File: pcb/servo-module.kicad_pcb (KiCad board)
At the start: 4 copper layers, 50 x 30 mm, 44 parts, among them J1 AVR-UPDI-6, J2 QWICC, J3 Power, J4 INPUT, J5 PWM1, J6 PWM2, J7 PWM3, J8 PWM4, U2 ATTINY1616MNR

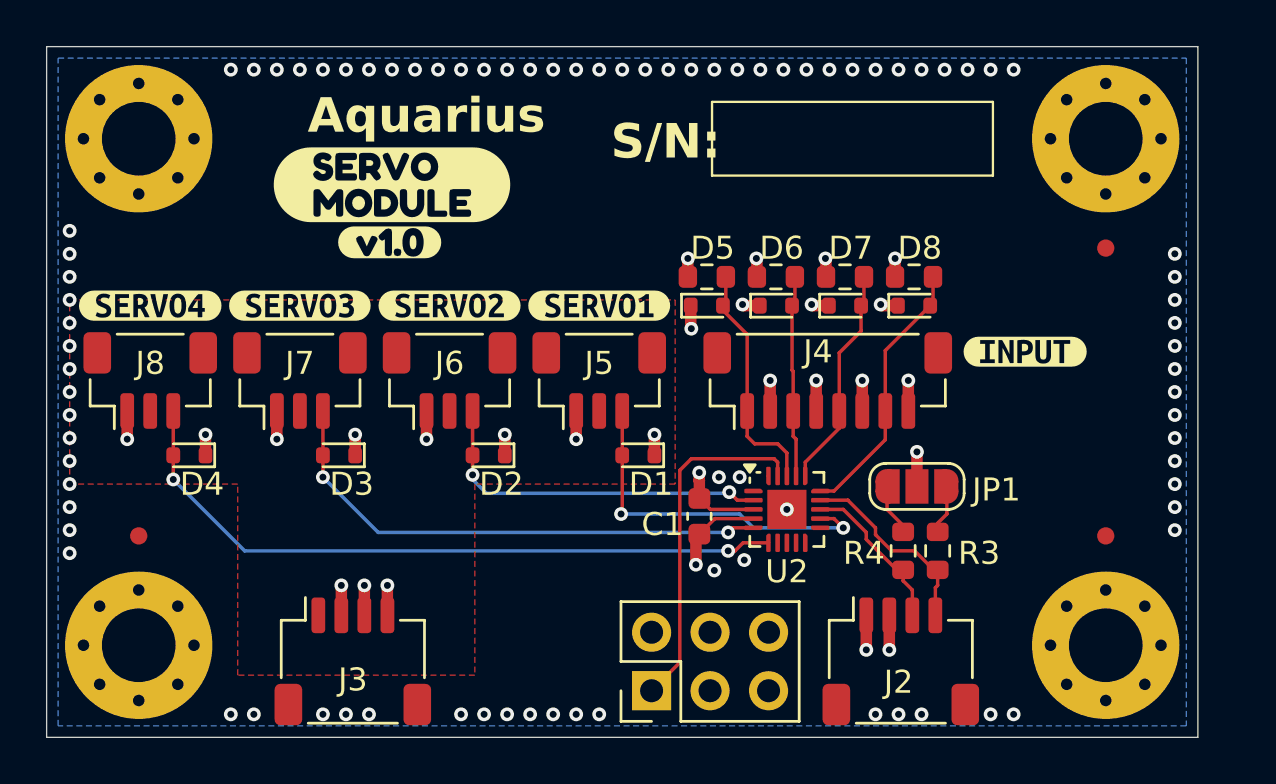
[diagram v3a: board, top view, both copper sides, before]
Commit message: Made multi-sheet; changed LEDs to WS2812; rerouted whole board
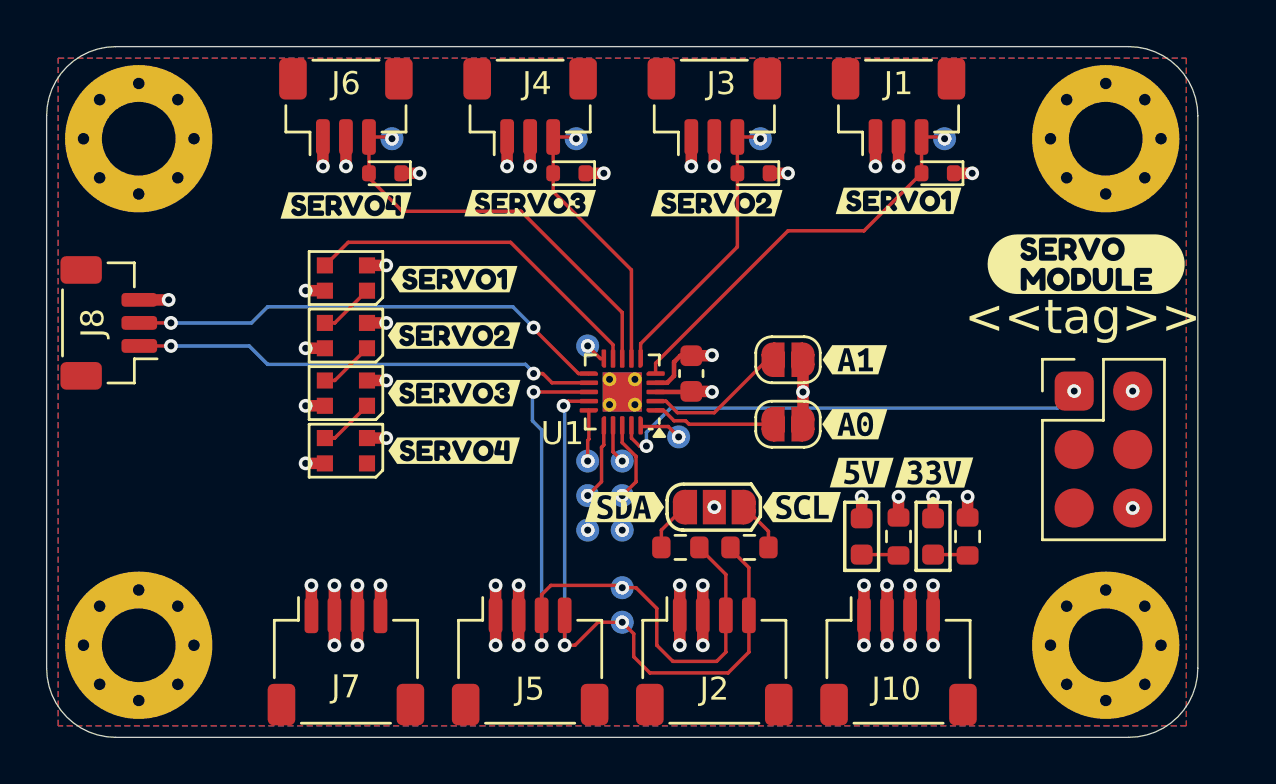
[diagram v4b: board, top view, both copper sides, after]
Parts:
- removed FID1, FID2, FID3: Fiducial, Fiducial:Fiducial_0.75mm_Mask1.5mm
- removed LOGO5: Logo_Open_Hardware_Small, Symbol:OSHW-Logo_5.7x6mm_SilkScreen
- removed R5, R6, R7, R8: 10K, Resistor_SMD:R_0603_1608Metric
- removed U2: ATTINY1616MNR, Package_DFN_QFN:VQFN-20-1EP_3x3mm_P0.4mm_EP1.7x1.7mm
- removed kibuzzard-67E4BAC2: G***, kibuzzard-67E4BAC2
- removed kibuzzard-67E4BADC: G***, kibuzzard-67E4BADC
- removed kibuzzard-67E9F1A1: G***, kibuzzard-67E9F1A1
- removed kibuzzard-67E9F1AC: G***, kibuzzard-67E9F1AC
- removed kibuzzard-67E9F1C4: G***, kibuzzard-67E9F1C4
- removed kibuzzard-67E9F26B: G***, kibuzzard-67E9F26B
- removed kibuzzard-67E9F303: G***, kibuzzard-67E9F303
- removed kibuzzard-67F88258: G***, kibuzzard-67F88258
- removed kibuzzard-67F8826B: G***, kibuzzard-67F8826B
- added D10: PESD5V0S1BB, CRGM Passive:D_SOD-523, F.Cu at (64.7, 140.5)
- added D9: PESD5V0S1BB, CRGM Passive:D_SOD-523, F.Cu at (72.7, 140.5)
- added J10: Power Out, CRGM Connector:JST_SH_SM04B-SRSS-TB_1x04-1MP_P1.00mm_Horizontal, F.Cu at (87.0, 161.7)
- added J9: AVR-UPDI-6, CRGM Connector:PinHeader_2x03_P2.54mm_Vertical_SMD, F.Cu at (94.6, 150.0)
- added JP2: A0, CRGM Connector:SolderJumper-2_P1.3mm_Open_RoundedPad1.0x1.5mm, F.Cu at (82.2, 151.4)
- added JP3: A1, CRGM Connector:SolderJumper-2_P1.3mm_Open_RoundedPad1.0x1.5mm, F.Cu at (82.2, 148.6)
- added LOGO2: ~, CRGM Logos:FNWW Face 8mm, B.Cu at (56.8, 151.9)
- added R1: 4.7K, Resistor_SMD:R_0603_1608Metric, F.Cu at (77.5, 156.8)
- added R2: 4.7K, Resistor_SMD:R_0603_1608Metric, F.Cu at (80.5, 156.8)
- added TP1: PA1, CRGM Mechanical:TestPoint_Pad_D1.0mm, B.Cu at (77.5, 151.9)
- added TP10: UPDI, CRGM Mechanical:TestPoint_Pad_D1.0mm, B.Cu at (94.6, 150.0)
- added TP11: V33, CRGM Mechanical:TestPoint_Pad_D1.0mm, B.Cu at (73.5, 156.0)
- added TP12: GND, CRGM Mechanical:TestPoint_Pad_D1.0mm, B.Cu at (75.0, 156.0)
- added TP13: PB3, CRGM Mechanical:TestPoint_Pad_D1.0mm, B.Cu at (73.5, 148.0)
- added TP14: PC3, CRGM Mechanical:TestPoint_Pad_D1.0mm, B.Cu at (75.0, 154.5)
- added TP15: PC2, CRGM Mechanical:TestPoint_Pad_D1.0mm, B.Cu at (75.0, 153.0)
- added TP2: PC0, CRGM Mechanical:TestPoint_Pad_D1.0mm, B.Cu at (73.5, 153.0)
- added TP3: PC1, CRGM Mechanical:TestPoint_Pad_D1.0mm, B.Cu at (73.5, 154.5)
- added TP4: SERVO1, CRGM Mechanical:TestPoint_Pad_D1.0mm, B.Cu at (89.0, 139.0)
- added TP5: SERVO2, CRGM Mechanical:TestPoint_Pad_D1.0mm, B.Cu at (81.0, 139.0)
- added TP6: SERVO3, CRGM Mechanical:TestPoint_Pad_D1.0mm, B.Cu at (73.0, 139.0)
- added TP7: SCL, CRGM Mechanical:TestPoint_Pad_D1.0mm, B.Cu at (75.0, 160.0)
- added TP8: SDA, CRGM Mechanical:TestPoint_Pad_D1.0mm, B.Cu at (75.0, 158.5)
- added TP9: SERVO3, CRGM Mechanical:TestPoint_Pad_D1.0mm, B.Cu at (65.0, 139.0)
- added U1: ATtiny1616-MNR, CRG Makes:VQFN-20-1EP_3x3mm_P0.4mm_EP1.7x1.7mm_ThermalVias, F.Cu at (75.0, 150.0)
- added kibuzzard-68583EA9: G***, kibuzzard-68583EA9, F.Cu at (67.7, 145.1)
- added kibuzzard-68583EC3: G***, kibuzzard-68583EC3, F.Cu at (87.0, 141.7)
- added kibuzzard-68583EE4: G***, kibuzzard-68583EE4, F.Cu at (79.1, 141.8)
- added kibuzzard-68583EEB: G***, kibuzzard-68583EEB, F.Cu at (71.0, 141.8)
- added kibuzzard-68583F01: G***, kibuzzard-68583F01, F.Cu at (63.0, 141.9)
- added kibuzzard-68583F18: G***, kibuzzard-68583F18, F.Cu at (67.7, 152.6)
- added kibuzzard-68583F22: G***, kibuzzard-68583F22, F.Cu at (67.7, 150.1)
- added kibuzzard-68583F28: G***, kibuzzard-68583F28, F.Cu at (67.7, 147.6)
- added kibuzzard-6858441E: G***, kibuzzard-6858441E, F.Cu at (85.4, 153.5)
- added kibuzzard-6858446E: G***, kibuzzard-6858446E, F.Cu at (88.5, 153.5)
- added kibuzzard-68584599: G***, kibuzzard-68584599, F.Cu at (75.1, 155.0)
- added kibuzzard-685845A0: G***, kibuzzard-685845A0, F.Cu at (82.8, 155.0)
- added kibuzzard-685845CF: G***, kibuzzard-685845CF, F.Cu at (85.1, 151.4)
- added kibuzzard-685845E1: G***, kibuzzard-685845E1, F.Cu at (85.1, 148.6)
- added kibuzzard-68585AB3: G***, kibuzzard-68585AB3, F.Cu at (95.2, 144.4)
- added kibuzzard-68585C25: G***, kibuzzard-68585C25, B.Cu at (82.8, 143.6)
- added kibuzzard-685861B4: G***, kibuzzard-685861B4, B.Cu at (76.1, 148.0)
- added kibuzzard-685861D3: G***, kibuzzard-685861D3, B.Cu at (72.5, 158.5)
- added kibuzzard-685861D9: G***, kibuzzard-685861D9, B.Cu at (72.7, 160.0)
- added kibuzzard-68586205: G***, kibuzzard-68586205, B.Cu at (79.7, 151.9)
- added kibuzzard-6858621A: G***, kibuzzard-6858621A, B.Cu at (77.2, 154.5)
- added kibuzzard-68586228: G***, kibuzzard-68586228, B.Cu at (77.2, 153.2)
- added kibuzzard-68586245: G***, kibuzzard-68586245, B.Cu at (77.5, 156.0)
- added kibuzzard-68586251: G***, kibuzzard-68586251, B.Cu at (71.2, 153.0)
- added kibuzzard-68586260: G***, kibuzzard-68586260, B.Cu at (71.4, 154.5)
- added kibuzzard-68586282: G***, kibuzzard-68586282, B.Cu at (71.2, 156.0)
- D2: value PESD5V0S1BB -> Orange; footprint CRGM Passive:D_SOD-523 -> LED_SMD:LED_0603_1608Metric
- D3: value PESD5V0S1BB -> Blue; footprint CRGM Passive:D_SOD-523 -> LED_SMD:LED_0603_1608Metric
- D4, D5, D6, D7: value PESD5V0S1BB -> WS2812B-2020; footprint CRGM Passive:D_SOD-523 -> LED_SMD:LED_WS2812B-2020_PLCC4_2.0x2.0mm
- J1: value AVR-UPDI-6 -> ~; footprint Connector_PinHeader_2.54mm:PinHeader_2x03_P2.54mm_Vertical -> CRGM Connector:JST_SH_BM03B-SRSS-TB_1x03-1MP_P1.00mm_Vertical
- J2: footprint Connector_JST:JST_SH_SM04B-SRSS-TB_1x04-1MP_P1.00mm_Horizontal -> CRGM Connector:JST_SH_SM04B-SRSS-TB_1x04-1MP_P1.00mm_Horizontal
- J3: value Power -> ~; footprint Connector_JST:JST_SH_SM04B-SRSS-TB_1x04-1MP_P1.00mm_Horizontal -> CRGM Connector:JST_SH_BM03B-SRSS-TB_1x03-1MP_P1.00mm_Vertical
- J4: value INPUT -> ~; footprint Connector_JST:JST_SH_BM08B-SRSS-TB_1x08-1MP_P1.00mm_Vertical -> CRGM Connector:JST_SH_BM03B-SRSS-TB_1x03-1MP_P1.00mm_Vertical
- J5: value PWM1 -> QWICC; footprint Connector_JST:JST_SH_BM03B-SRSS-TB_1x03-1MP_P1.00mm_Vertical -> CRGM Connector:JST_SH_SM04B-SRSS-TB_1x04-1MP_P1.00mm_Horizontal
- J6: value PWM2 -> ~; footprint Connector_JST:JST_SH_BM03B-SRSS-TB_1x03-1MP_P1.00mm_Vertical -> CRGM Connector:JST_SH_BM03B-SRSS-TB_1x03-1MP_P1.00mm_Vertical
- J7: value PWM3 -> Power In; footprint Connector_JST:JST_SH_BM03B-SRSS-TB_1x03-1MP_P1.00mm_Vertical -> CRGM Connector:JST_SH_SM04B-SRSS-TB_1x04-1MP_P1.00mm_Horizontal
- J8: value PWM4 -> ~; footprint Connector_JST:JST_SH_BM03B-SRSS-TB_1x03-1MP_P1.00mm_Vertical -> CRGM Connector:JST_SH_BM03B-SRSS-TB_1x03-1MP_P1.00mm_Vertical
- JP1: footprint Jumper:SolderJumper-3_P1.3mm_Open_RoundedPad1.0x1.5mm_NumberLabels -> CRGM Connector:SolderJumper-3_P1.3mm_Open_RoundedPad1.0x1.5mm
- LOGO1: footprint CRGM Logos:Aquarius Logo 10mm -> CRGM Logos:Aquarius Logo 8mm
- LOGO3: value ~ -> Logo_Open_Hardware_Small; footprint CRGM Logos:FNWW Face 10mm -> Symbol:OSHW-Logo_5.7x6mm_SilkScreen
- R3: value 10K -> 4.7k
- R4: value 10K -> 1k
- moved J3 28.8 mm to (79.0, 137.6)
- moved J1 27.5 mm to (87.0, 137.6), turned to 0 degrees
- moved D3 26.0 mm to (88.5, 156.3), turned to -90 degrees
- moved LOGO1 22.7 mm to (93.4, 146.0)
- moved D7 22.6 mm to (63.0, 152.6), turned to 180 degrees
- moved D6 19.1 mm to (63.0, 150.1), turned to 180 degrees
- moved LOGO3 17.9 mm to (65.5, 154.8)
- moved D1 17.9 mm to (88.7, 140.5)
- moved J4 17.6 mm to (71.0, 137.6)
- moved D2 16.6 mm to (85.4, 156.3), turned to -90 degrees
- moved D5 15.7 mm to (63.0, 147.6), turned to 180 degrees
- moved J6 12.7 mm to (63.0, 137.6)
- moved J5 12.6 mm to (71.0, 161.7)
- moved J7 12.4 mm to (63.0, 161.7)
- moved D4 10.3 mm to (63.0, 145.1)
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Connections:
- D1 pad 2: /PWM1 -> SERVO1
- D2 pad 2: /PWM2 -> /Indicators/V5LED
- D3 pad 2: /PWM3 -> /Indicators/V3.3LED
- D4 pad 1: GND -> Net-(D4-DOUT)
- D4 pad 2: /PWM4 -> GND
- D5 pad 1: GND -> Net-(D5-DOUT)
- D5 pad 2: /IN4 -> GND
- D6 pad 1: GND -> Net-(D6-DOUT)
- D6 pad 2: /IN3 -> GND
- D7 pad 1: GND -> unconnected-(D7-DOUT-Pad1)
- D7 pad 2: /IN2 -> GND
- D8 pad 2: /IN1 -> SERVO2
- J1 pad 1: /UPDI -> GND
- J1 pad 2: +3.3V -> +5V
- J1 pad 3: unconnected-(J1-NC-Pad3) -> SERVO1
- J2 pad 3: /SDA -> SDA
- J2 pad 4: /SCL -> SCL
- J3 pad 1: +5V -> GND
- J3 pad 2: GND -> +5V
- J3 pad 3: GND -> SERVO2
- J4 pad 1: /IN4 -> GND
- J4 pad 2: GND -> +5V
- J4 pad 3: /IN3 -> SERVO3
- J5 pad 2: +5V -> +3.3V
- J5 pad 3: /PWM1 -> SDA
- J6 pad 3: /PWM2 -> SERVO4
- J7 pad 1: GND -> +5V
- J7 pad 2: +5V -> GND
- J7 pad 3: /PWM3 -> GND
- J8 pad 1: GND -> TXD
- J8 pad 2: +5V -> RXD
- J8 pad 3: /PWM4 -> GND
- R3 pad 1: /SCL -> +5V
- R3 pad 2: Net-(JP1-A) -> /Indicators/V5LED
- R4 pad 1: /SDA -> +3.3V
- R4 pad 2: Net-(JP1-B) -> /Indicators/V3.3LED
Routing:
- net SDA: track 0.00 -> 31.4 mm, vias 0 -> 3
- net /PWM4: track 30.3 -> 0.00 mm, vias 2 -> 0
- net SCL: track 0.00 -> 28.1 mm, vias 0 -> 3
- net /PWM3: track 22.7 -> 0.00 mm, vias 2 -> 0
- net UPDI: track 0.00 -> 21.3 mm, vias 0 -> 2
- net RXD: track 0.00 -> 21.0 mm, vias 0 -> 2
- net TXD: track 0.00 -> 20.2 mm, vias 0 -> 2
- net SERVO4: track 0.00 -> 18.2 mm, vias 0 -> 1
- net SERVO1: track 0.00 -> 18.2 mm, vias 0 -> 1
- net /UPDI: track 15.7 -> 0.00 mm
- net /PWM2: track 15.6 -> 0.00 mm, vias 2 -> 0
- net /PWM1: track 15.6 -> 0.00 mm, vias 2 -> 0
- net STATUS_LEDS: track 0.00 -> 15.4 mm
- net SERVO2: track 0.00 -> 12.4 mm, vias 0 -> 1
- net SERVO3: track 0.00 -> 12.2 mm, vias 0 -> 1
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- added copper zone on In1.Cu, net +5V
- added copper zone on F.Cu, net GND
- removed copper zone on F.Cu, net +5V
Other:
- outline, holes or cut-outs redrawn
- board text added: "<<hash>>"
- board text added: "<<tag>>"
- board text added: "x 4"
- board text removed: "Aquarius"
- board text removed: "S/N:"
